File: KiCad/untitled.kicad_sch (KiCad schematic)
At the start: 27 parts, among them J1 CONNECTOR_MOTOR, Q1 IRLZ44N, Q2 IRLZ44N, Q3 IRLZ44N, Q4 IRLZ44N, Q5 IRLZ44N, Q6 IRLZ44N, Q7 IRLZ44N, U1 LM2596S-5, U2 LM1117MP-3.3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

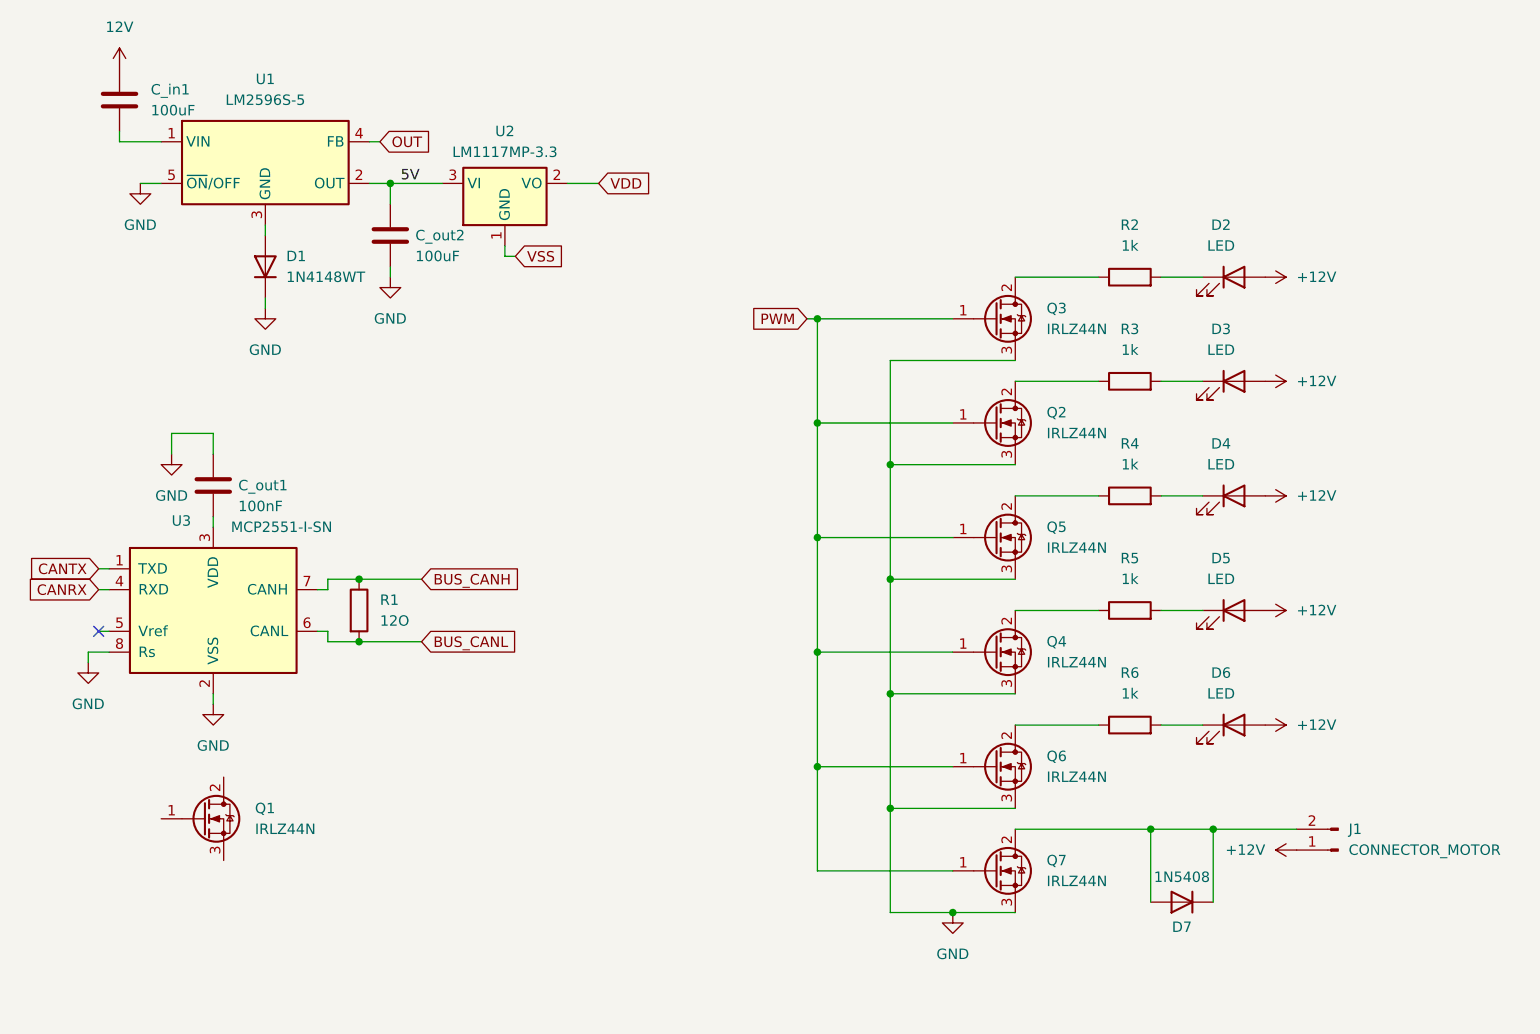
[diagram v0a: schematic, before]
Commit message: llums bé amb les etiquetes bé
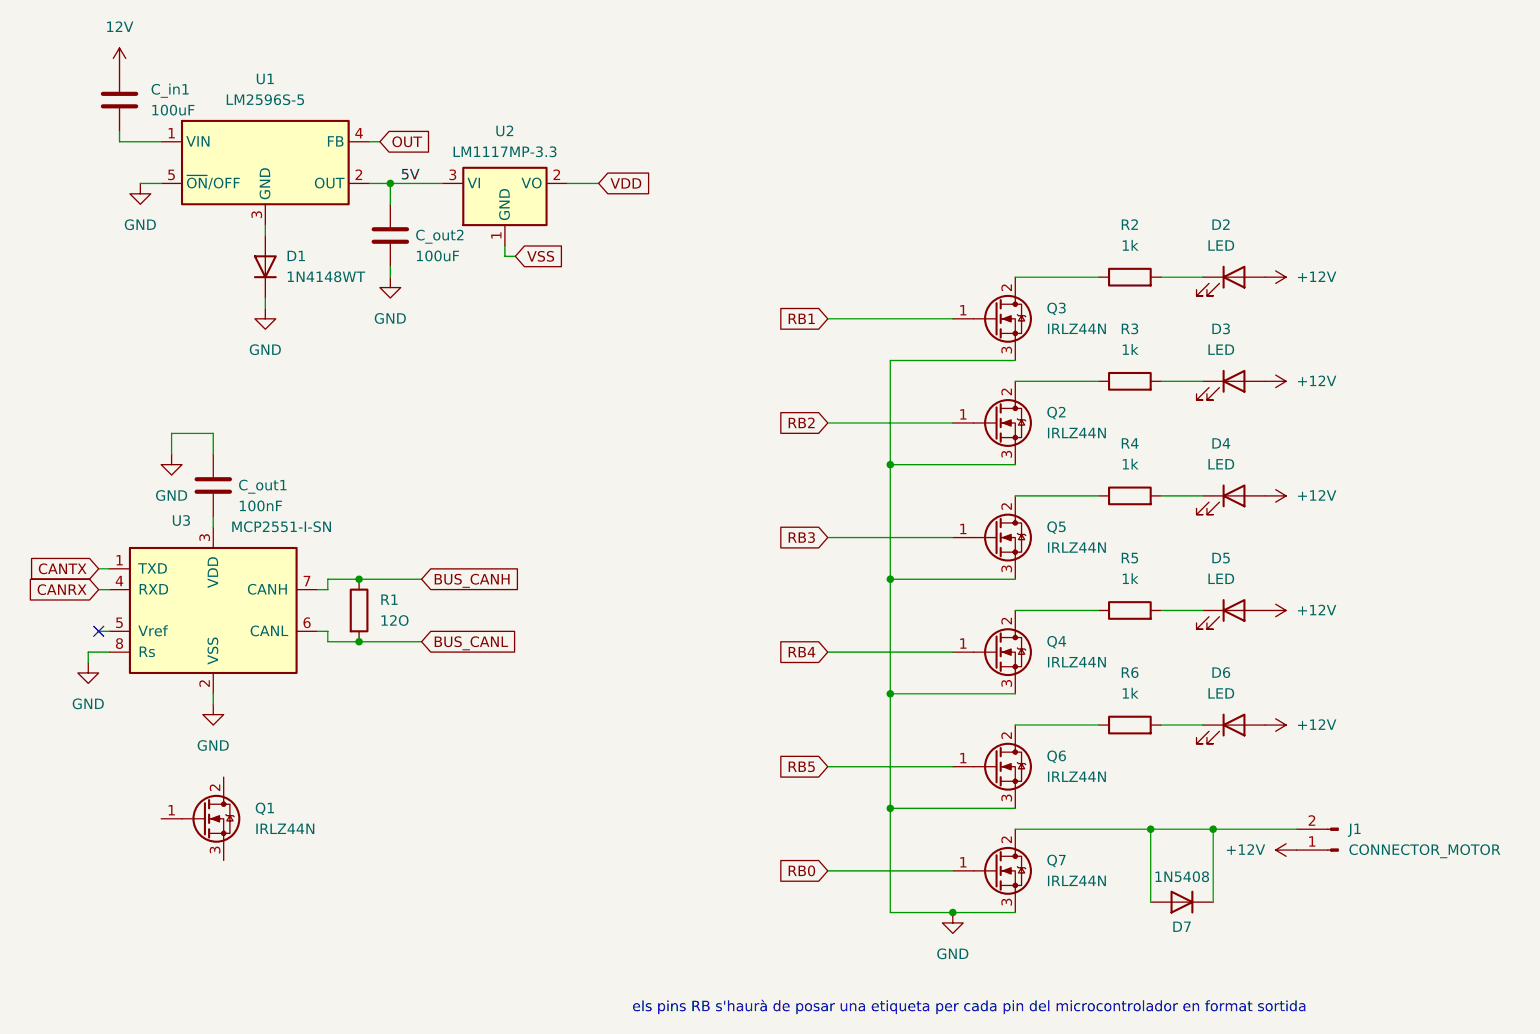
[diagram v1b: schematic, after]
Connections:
- removed net PWM: Q2.1 (G), Q3.1 (G), Q4.1 (G), Q5.1 (G), Q6.1 (G), Q7.1 (G)
- new net RB0: Q7.1 (G)
- new net RB1: Q3.1 (G)
- new net RB2: Q2.1 (G)
- new net RB3: Q5.1 (G)
- new net RB4: Q4.1 (G)
- new net RB5: Q6.1 (G)
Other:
- note added: "els pins RB s'haurà de posar una etiqueta per cada pin del microcontrolador en format sortida"
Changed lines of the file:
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@@
 	(generator_version "9.0")
 	(paper "A4")
-	(junction
-		(at 115.57 60.96)
-		(diameter 0)
-		(color 0 0 0 0)
+	(text "els pins RB s'haurà de posar una etiqueta per cada pin del microcontrolador en format sortida\n"
+		(exclude_from_sim no)
+		(at 134.112 145.034 0)
+		(effects
+			(font
+				(size 1.27 1.27)
+			)
+		)
 	)
 	(junction
@@
 	)
 	(junction
-		(at 115.57 73.66)
-		(diameter 0)
-		(color 0 0 0 0)
-	)
-	(junction
 		(at 156.21 123.19)
 		(diameter 0)
@@
 	)
 	(junction
-		(at 115.57 115.57)
-		(diameter 0)
-		(color 0 0 0 0)
-	)
-	(junction
 		(at 132.08 133.35)
 		(diameter 0)
@@
 	)
 	(junction
-		(at 115.57 101.6)
-		(diameter 0)
-		(color 0 0 0 0)
-	)
-	(junction
 		(at 124.46 120.65)
 		(diameter 0)
@@
 	)
 	(junction
-		(at 115.57 87.63)
-		(diameter 0)
-		(color 0 0 0 0)
-	)
-	(junction
 		(at 124.46 78.74)
 		(diameter 0)
@@
 	(wire
 		(pts
-			(xy 132.08 128.27) (xy 115.57 128.27)
-		)
-		(stroke
-			(width 0)
-			(type default)
-		)
-	)
-	(wire
-		(pts
 			(xy 156.21 123.19) (xy 163.83 123.19)
 		)
@@
 	(wire
 		(pts
-			(xy 132.08 101.6) (xy 115.57 101.6)
-		)
-		(stroke
-			(width 0)
-			(type default)
-		)
-	)
-	(wire
-		(pts
-			(xy 115.57 73.66) (xy 115.57 60.96)
-		)
-		(stroke
-			(width 0)
-			(type default)
-		)
-	)
-	(wire
-		(pts
-			(xy 115.57 60.96) (xy 132.08 60.96)
-		)
-		(stroke
-			(width 0)
-			(type default)
-		)
-	)
-	(wire
-		(pts
 			(xy 36.83 77.47) (xy 36.83 74.93)
 		)
@@
 	(wire
 		(pts
-			(xy 132.08 73.66) (xy 115.57 73.66)
-		)
-		(stroke
-			(width 0)
-			(type default)
-		)
-	)
-	(wire
-		(pts
 			(xy 55.88 93.98) (xy 54.61 93.98)
 		)
@@
 	(wire
 		(pts
-			(xy 114.3 60.96) (xy 115.57 60.96)
-		)
-		(stroke
-			(width 0)
-			(type default)
-		)
-	)
-	(wire
-		(pts
 			(xy 124.46 78.74) (xy 139.7 78.74)
 		)
@@
 	(wire
 		(pts
+			(xy 116.84 60.96) (xy 132.08 60.96)
+		)
+		(stroke
+			(width 0)
+			(type default)
+		)
+	)
+	(wire
+		(pts
 			(xy 124.46 78.74) (xy 124.46 92.71)
 		)
@@
 	(wire
 		(pts
+			(xy 116.84 128.27) (xy 132.08 128.27)
+		)
+		(stroke
+			(width 0)
+			(type default)
+		)
+	)
+	(wire
+		(pts
 			(xy 27.94 91.44) (xy 29.21 91.44)
 		)
@@
 	(wire
 		(pts
+			(xy 116.84 101.6) (xy 132.08 101.6)
+		)
+		(stroke
+			(width 0)
+			(type default)
+		)
+	)
+	(wire
+		(pts
 			(xy 60.96 44.45) (xy 63.5 44.45)
 		)
@@
 	(wire
 		(pts
-			(xy 132.08 87.63) (xy 115.57 87.63)
-		)
-		(stroke
-			(width 0)
-			(type default)
-		)
-	)
-	(wire
-		(pts
 			(xy 26.67 102.87) (xy 26.67 101.6)
 		)
@@
 	(wire
 		(pts
-			(xy 115.57 101.6) (xy 115.57 87.63)
-		)
-		(stroke
-			(width 0)
-			(type default)
-		)
-	)
-	(wire
-		(pts
 			(xy 139.7 68.58) (xy 149.86 68.58)
 		)
@@
 	(wire
 		(pts
-			(xy 115.57 87.63) (xy 115.57 73.66)
-		)
-		(stroke
-			(width 0)
-			(type default)
-		)
-	)
-	(wire
-		(pts
 			(xy 48.26 59.69) (xy 48.26 58.42)
 		)
@@
 	(wire
 		(pts
-			(xy 132.08 115.57) (xy 115.57 115.57)
-		)
-		(stroke
-			(width 0)
-			(type default)
-		)
-	)
-	(wire
-		(pts
-			(xy 115.57 128.27) (xy 115.57 115.57)
-		)
-		(stroke
-			(width 0)
-			(type default)
-		)
-	)
-	(wire
-		(pts
 			(xy 27.94 99.06) (xy 29.21 99.06)
 		)
@@
 	(wire
 		(pts
-			(xy 115.57 115.57) (xy 115.57 101.6)
+			(xy 116.84 87.63) (xy 132.08 87.63)
+		)
+		(stroke
+			(width 0)
+			(type default)
+		)
+	)
+	(wire
+		(pts
+			(xy 116.84 115.57) (xy 132.08 115.57)
 		)
 		(stroke
@@
 		(pts
 			(xy 63.5 54.61) (xy 63.5 55.88)
+		)
+		(stroke
+			(width 0)
+			(type default)
+		)
+	)
+	(wire
+		(pts
+			(xy 116.84 73.66) (xy 132.08 73.66)
 		)
 		(stroke
@@
 		)
 	)
+	(global_label "RB3"
+		(shape input)
+		(at 116.84 87.63 180)
+		(fields_autoplaced yes)
+		(effects
+			(font
+				(size 1.27 1.27)
+			)
+			(justify right)
+		)
+		(property "Intersheetrefs" "${INTERSHEET_REFS}"
+			(at 110.1053 87.63 0)
+			(effects
+				(font
+					(size 1.27 1.27)
+				)
+				(justify right)
+				(hide yes)
+			)
+		)
+	)
+	(global_label "RB1"
+		(shape input)
+		(at 116.84 60.96 180)
+		(fields_autoplaced yes)
+		(effects
+			(font
+				(size 1.27 1.27)
+			)
+			(justify right)
+		)
+		(property "Intersheetrefs" "${INTERSHEET_REFS}"
+			(at 110.1053 60.96 0)
+			(effects
+				(font
+					(size 1.27 1.27)
+				)
+				(justify right)
+				(hide yes)
+			)
+		)
+	)
 	(global_label "BUS_CANH"
 		(shape input)
@@
 		)
 	)
+	(global_label "RB2"
+		(shape input)
+		(at 116.84 73.66 180)
+		(fields_autoplaced yes)
+		(effects
+			(font
+				(size 1.27 1.27)
+			)
+			(justify right)
+		)
+		(property "Intersheetrefs" "${INTERSHEET_REFS}"
+			(at 110.1053 73.66 0)
+			(effects
+				(font
+					(size 1.27 1.27)
+				)
+				(justify right)
+				(hide yes)
+			)
+		)
+	)
 	(global_label "CANRX"
 		(shape input)
@@
 		)
 	)
-	(global_label "PWM"
-		(shape input)
-		(at 114.3 60.96 180)
+	(global_label "RB5"
+		(shape input)
+		(at 116.84 115.57 180)
 		(fields_autoplaced yes)
 		(effects
@@
 		)
 		(property "Intersheetrefs" "${INTERSHEET_REFS}"
-			(at 107.142 60.96 0)
+			(at 110.1053 115.57 0)
 			(effects
 				(font
@@
 		)
 	)
+	(global_label "RB4"
+		(shape input)
+		(at 116.84 101.6 180)
+		(fields_autoplaced yes)
+		(effects
+			(font
+				(size 1.27 1.27)
+			)
+			(justify right)
+		)
+		(property "Intersheetrefs" "${INTERSHEET_REFS}"
+			(at 110.1053 101.6 0)
+			(effects
+				(font
+					(size 1.27 1.27)
+				)
+				(justify right)
+				(hide yes)
+			)
+		)
+	)
 	(global_label "OUT"
 		(shape input)
@@
 				(hide yes)
 			)
+		)
+	)
+	(global_label "RB0"
+		(shape input)
+		(at 116.84 128.27 180)
+		(fields_autoplaced yes)
+		(effects
+			(font
+				(size 1.27 1.27)
+			)
+			(justify right)
+		)
+		(property "Intersheetrefs" "${INTERSHEET_REFS}"
+			(at 110.1053 128.27 0)
+			(effects
+				(font
+					(size 1.27 1.27)
+				)
+				(justify right)
+				(hide yes)
+			)
